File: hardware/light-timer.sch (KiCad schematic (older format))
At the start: 4 parts, among them P1 Power Connector, P2 Pushbutton Connector, P3 Relay Connector, U1 LeoStick

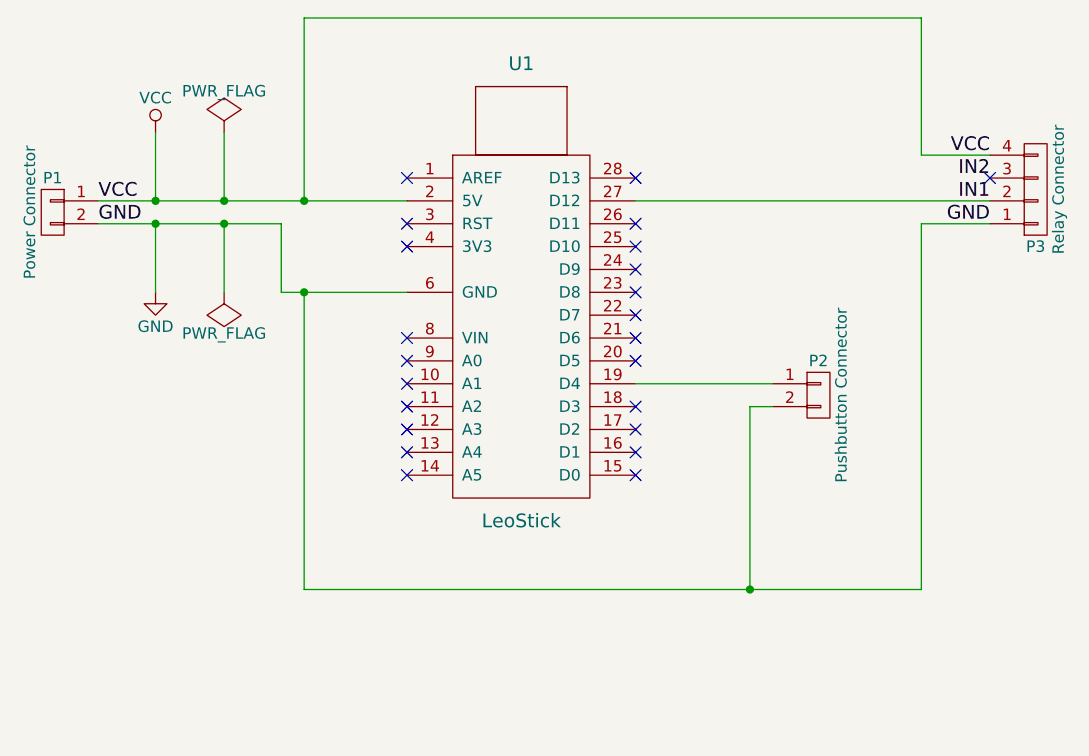
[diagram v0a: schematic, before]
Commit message: Add duration DIP switches, board layout
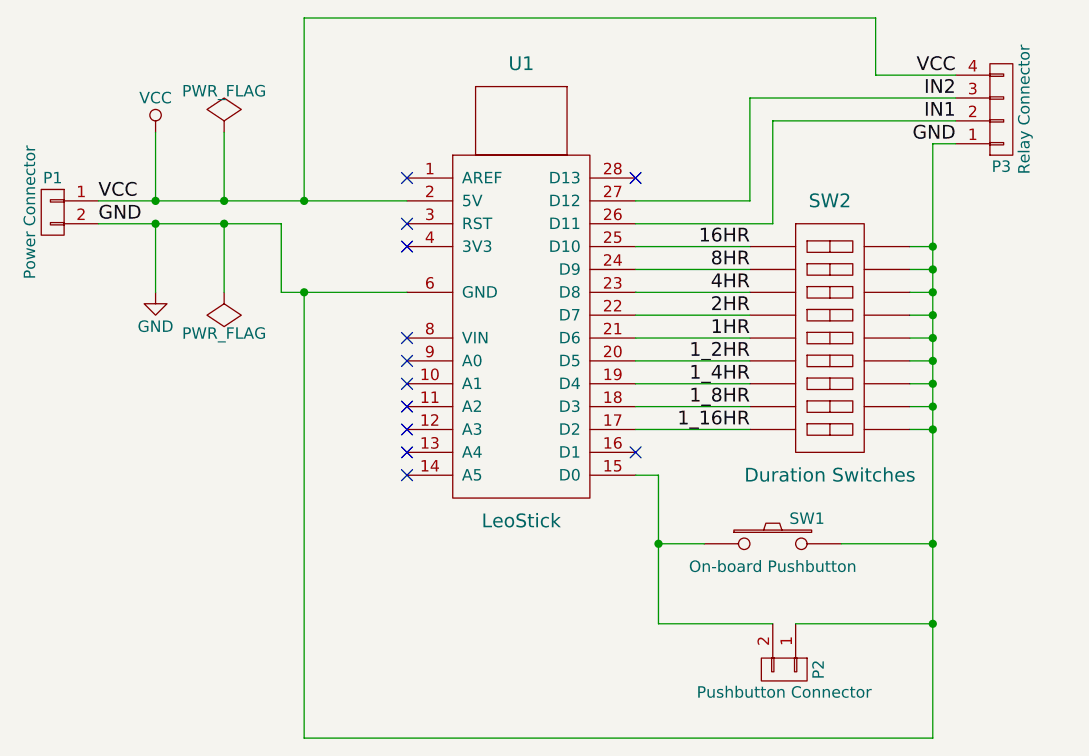
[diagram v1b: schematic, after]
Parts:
- added SW1: On-board Pushbutton, Buttons_Switches_ThroughHole:SW_PUSH-12mm, symbol SW_PUSH
- added SW2: Duration Switches, Housings_DIP:DIP-18_W7.62mm, symbol DIP_SW_9
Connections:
- net GND: now also P2.1 (P1), SW1.2, SW2.10, SW2.11, SW2.12, SW2.13, SW2.14, SW2.15, SW2.16, SW2.17, SW2.18; no longer P2.2 (P2)
- net IN1: now also U1.26 (D11); no longer U1.27 (D12)
- net IN2: now also U1.27 (D12)
- net at U1.15 (D0): now also P2.2 (P2), SW1.1
- net 1_16HR: now reaches U1.17 (D2)
- net 1_16HR: now also SW2.9
- net 1_8HR: now reaches U1.18 (D3)
- net 1_8HR: now also SW2.8
- net 1_4HR: now reaches U1.19 (D4)
- net 1_4HR: now also SW2.7; no longer P2.1 (P1)
- net 1_2HR: now reaches U1.20 (D5)
- net 1_2HR: now also SW2.6
- net 1HR: now reaches U1.21 (D6)
- net 1HR: now also SW2.5
- net 2HR: now reaches U1.22 (D7)
- net 2HR: now also SW2.4
- net 4HR: now reaches U1.23 (D8)
- net 4HR: now also SW2.3
- net 8HR: now reaches U1.24 (D9)
- net 8HR: now also SW2.2
- net 16HR: now reaches U1.25 (D10)
- net 16HR: now also SW2.1
- no-connect marks 23 -> 12
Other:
- moved on the sheet: P2, P3
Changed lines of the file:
@@
 L CONN_01X04 P3
 U 1 1 586445BA
-P 5650 2750
-F 0 "P3" H 5650 3000 50  0000 C CNN
-F 1 "Relay Connector" V 5750 2750 50  0000 C CNN
-F 2 "Socket_Strips:Socket_Strip_Straight_1x04" H 5650 2750 50  0001 C CNN
-F 3 "" H 5650 2750 50  0000 C CNN
-	1    5650 2750
+P 5500 2400
+F 0 "P3" H 5500 2650 50  0000 C CNN
+F 1 "Relay Connector" V 5600 2400 50  0000 C CNN
+F 2 "Socket_Strips:Socket_Strip_Straight_1x04" H 5500 2400 50  0001 C CNN
+F 3 "" H 5500 2400 50  0000 C CNN
+	1    5500 2400
 	1    0    0    1
 $EndComp
-Text Label 5450 2900 2    60   ~ 0
+Text Label 5300 2550 2    60   ~ 0
 GND
-Text Label 5450 2800 2    60   ~ 0
+Text Label 5300 2450 2    60   ~ 0
 IN1
-Text Label 5450 2700 2    60   ~ 0
+Text Label 5300 2350 2    60   ~ 0
 IN2
-Text Label 5450 2600 2    60   ~ 0
+Text Label 5300 2250 2    60   ~ 0
 VCC
 $Comp
 L CONN_01X02 P2
 U 1 1 5864463F
-P 4700 3650
-F 0 "P2" H 4700 3800 50  0000 C CNN
-F 1 "Pushbutton Connector" V 4800 3650 50  0000 C CNN
-F 2 "Socket_Strips:Socket_Strip_Straight_1x02" H 4700 3650 50  0001 C CNN
-F 3 "" H 4700 3650 50  0000 C CNN
-	1    4700 3650
-	1    0    0    -1
+P 4550 4850
+F 0 "P2" H 4550 5000 50  0000 C CNN
+F 1 "Pushbutton Connector" V 4650 4850 50  0000 C CNN
+F 2 "Socket_Strips:Socket_Strip_Straight_1x02" H 4550 4850 50  0001 C CNN
+F 3 "" H 4550 4850 50  0000 C CNN
+	1    4550 4850
+	0    1    1    0
 $EndComp
 $Comp
@@
 Connection ~ 2100 2900
 Wire Wire Line
-	3900 2800 5450 2800
-Wire Wire Line
-	2450 2000 5150 2000
+	2450 2000 4950 2000
 Wire Wire Line
 	2450 2000 2450 2800
 Connection ~ 2450 2800
 Wire Wire Line
-	5450 2600 5150 2600
-Wire Wire Line
-	5150 2600 5150 2000
-Wire Wire Line
-	5450 2900 5150 2900
-Wire Wire Line
-	5150 4500 5150 2900
-Wire Wire Line
-	2450 4500 5150 4500
-Wire Wire Line
-	2450 4500 2450 3200
+	2450 5150 5200 5150
+Wire Wire Line
+	2450 5150 2450 3200
 Connection ~ 2450 3200
-Wire Wire Line
-	4500 3600 3900 3600
-Wire Wire Line
-	4500 3700 4400 3700
-Wire Wire Line
-	4400 3700 4400 4500
-Connection ~ 4400 4500
 NoConn ~ 2900 2700
 NoConn ~ 2900 2900
@@
 NoConn ~ 2900 3900
 NoConn ~ 2900 4000
-NoConn ~ 3900 4000
+NoConn ~ 3900 2700
+$Comp
+L DIP_SW_9 SW2
+U 1 1 5865ACE5
+P 4750 3400
+F 0 "SW2" H 4750 4000 60  0000 C CNN
+F 1 "Duration Switches" H 4750 2800 60  0000 C CNN
+F 2 "Housings_DIP:DIP-18_W7.62mm" H 4750 3400 60  0001 C CNN
+F 3 "" H 4750 3400 60  0000 C CNN
+	1    4750 3400
+	1    0    0    -1
+$EndComp
+Wire Wire Line
+	3900 3000 4400 3000
+Wire Wire Line
+	3900 3100 4400 3100
+Wire Wire Line
+	3900 3200 4400 3200
+Wire Wire Line
+	3900 3300 4400 3300
+Wire Wire Line
+	3900 3400 4400 3400
+Wire Wire Line
+	3900 3500 4400 3500
+Wire Wire Line
+	3900 3600 4400 3600
+Wire Wire Line
+	3900 3700 4400 3700
+Wire Wire Line
+	3900 3800 4400 3800
+Wire Wire Line
+	5100 3000 5200 3000
+Wire Wire Line
+	5200 5150 5200 2550
+Wire Wire Line
+	5100 3100 5200 3100
+Connection ~ 5200 3100
+Wire Wire Line
+	5100 3200 5200 3200
+Connection ~ 5200 3200
+Wire Wire Line
+	5100 3300 5200 3300
+Connection ~ 5200 3300
+Wire Wire Line
+	5100 3400 5200 3400
+Connection ~ 5200 3400
+Wire Wire Line
+	5100 3500 5200 3500
+Connection ~ 5200 3500
+Wire Wire Line
+	5100 3600 5200 3600
+Connection ~ 5200 3600
+Wire Wire Line
+	5100 3700 5200 3700
+Connection ~ 5200 3700
+Wire Wire Line
+	5100 3800 5200 3800
+Connection ~ 5200 3800
+Wire Wire Line
+	5300 2250 4950 2250
+Wire Wire Line
+	4950 2250 4950 2000
+Wire Wire Line
+	5300 2450 4500 2450
+Wire Wire Line
+	4500 2450 4500 2900
+Wire Wire Line
+	4500 2900 3900 2900
+Wire Wire Line
+	3900 2800 4400 2800
+Wire Wire Line
+	4400 2800 4400 2350
+Wire Wire Line
+	4400 2350 5300 2350
+Wire Wire Line
+	5200 2550 5300 2550
+Connection ~ 5200 3000
+$Comp
+L SW_PUSH SW1
+U 1 1 5865B215
+P 4500 4300
+F 0 "SW1" H 4650 4410 50  0000 C CNN
+F 1 "On-board Pushbutton" H 4500 4200 50  0000 C CNN
+F 2 "Buttons_Switches_ThroughHole:SW_PUSH-12mm" H 4500 4300 50  0001 C CNN
+F 3 "" H 4500 4300 50  0000 C CNN
+	1    4500 4300
+	1    0    0    -1
+$EndComp
+Wire Wire Line
+	3900 4000 4000 4000
+Wire Wire Line
+	4000 4000 4000 4650
+Connection ~ 4000 4300
+Wire Wire Line
+	4800 4300 5200 4300
+Connection ~ 5200 4300
+Wire Wire Line
+	4600 4650 5200 4650
+Connection ~ 5200 4650
 NoConn ~ 3900 3900
-NoConn ~ 3900 3800
-NoConn ~ 3900 3700
-NoConn ~ 3900 3500
-NoConn ~ 3900 3400
-NoConn ~ 3900 3300
-NoConn ~ 3900 3200
-NoConn ~ 3900 3100
-NoConn ~ 3900 3000
-NoConn ~ 3900 2900
-NoConn ~ 3900 2700
-NoConn ~ 5450 2700
+Text Label 4400 3000 2    60   ~ 0
+16HR
+Text Label 4400 3100 2    60   ~ 0
+8HR
+Text Label 4400 3200 2    60   ~ 0
+4HR
+Text Label 4400 3300 2    60   ~ 0
+2HR
+Text Label 4400 3400 2    60   ~ 0
+1HR
+Text Label 4400 3500 2    60   ~ 0
+1_2HR
+Text Label 4400 3600 2    60   ~ 0
+1_4HR
+Text Label 4400 3700 2    60   ~ 0
+1_8HR
+Text Label 4400 3800 2    60   ~ 0
+1_16HR
+Wire Wire Line
+	4000 4300 4200 4300
+Wire Wire Line
+	4000 4650 4500 4650
 $EndSCHEMATC
